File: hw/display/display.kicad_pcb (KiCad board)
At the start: 4 copper layers, 37 x 29 mm, 22 parts, among them J1 Input, J2 Output, U1 SN65LVDS822, U2 SN74LVC00ARGY

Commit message: temp commit for merge
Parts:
- added C13: 0.1uF, Capacitor_SMD:C_0603_1608Metric, F.Cu at (106.5, 77.8)
- added J3: Touch, Connector_FFC-FPC:Hirose_FH12-8S-0.5SH_1x08-1MP_P0.50mm_Horizontal, B.Cu at (108.4, 76.3)
- added J4: Spacer, footprints:Spacer, F.Cu at (145.5, 78.0)
- added J5: Spacer, footprints:Spacer, F.Cu at (145.5, 88.8)
- added R2: DNP, Resistor_SMD:R_0603_1608Metric, F.Cu at (118.5, 74.4)
- added R3: DNP, Resistor_SMD:R_0603_1608Metric, F.Cu at (118.5, 75.9)
- added R4: DNP, Resistor_SMD:R_0603_1608Metric, F.Cu at (118.5, 77.4)
- added R5: DNP, Resistor_SMD:R_0603_1608Metric, F.Cu at (117.2, 95.9)
- added R6: DNP, Resistor_SMD:R_0603_1608Metric, F.Cu at (115.7, 95.9)
- J1: footprint Connector_FFC-FPC:Hirose_FH12-26S-0.5SH_1x26-1MP_P0.50mm_Horizontal -> Connector_Molex:Molex_SlimStack_55560-0301_2x15_P0.50mm_Vertical
- J2: value Output -> Display; moved to B.Cu
- JP3: footprint Jumper:SolderJumper-2_P1.3mm_Bridged_RoundedPad1.0x1.5mm -> Jumper:SolderJumper-3_P1.3mm_Bridged12_RoundedPad1.0x1.5mm
- U2: footprint Package_DFN_QFN:Texas_S-PVQFN-N14_ThermalVias -> footprints:Texas_S-PVQFN-N14_ThermalVias
- moved C11 6.60 mm to (112.0, 81.8), turned to 180 degrees
- moved J2 3.00 mm to (139.1, 94.5)
- moved JP3 1.99 mm to (133.4, 98.5), turned to 0 degrees
- moved J1 1.75 mm to (114.8, 87.8), turned to 90 degrees
- moved C15 1.68 mm to (123.5, 97.2), turned to 270 degrees
- moved R1 1.68 mm to (125.0, 97.2)
- moved C14 0.75 mm to (129.8, 96.5)
- moved U2 0.75 mm to (128.2, 99.6)
- moved C12 0.25 mm to (138.6, 104.2)
- renumbered C13 to C14, C14 to C15
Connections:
- J1 pad 10: /LVDS_A2N -> /LVDS_A1N
- J1 pad 11: /LVDS_A2P -> CTP.RST
- J1 pad 12: GND -> /LVDS_A1P
- J1 pad 13: /LVDS_CLKN -> GND
- J1 pad 14: /LVDS_CLKP -> GND
- J1 pad 15: GND -> SPI.CS
- J1 pad 16: /LVDS_A3N -> /LVDS_A2N
- J1 pad 17: /LVDS_A3P -> SPI.SCK
- J1 pad 18: GND -> /LVDS_A2P
- J1 pad 19: SPI.CS -> SPI.MOSI
- J1 pad 20: SPI.SCK -> GND
- J1 pad 21: SPI.MOSI -> SPI.MISO
- J1 pad 22: SPI.MISO -> /LVDS_CLKN
- J1 pad 24: GND -> /LVDS_CLKP
- J1 pad 25: LED_K -> GND
- J1 pad 26: LED_A -> GND
- J1 pad 3: GND -> Net-(J1-Pad3)
- J1 pad 5: /LVDS_A0P -> CTP.SCL
- J1 pad 6: GND -> /LVDS_A0P
- J1 pad 7: /LVDS_A1N -> CTP.SDA
- J1 pad 8: /LVDS_A1P -> GND
- J1 pad 9: GND -> CTP.INT
- JP3 pad 1: /DISP_EN_IC -> Net-(JP3-Pad1)
- JP3 pad 2: Net-(JP3-Pad2) -> /DISP_DE_INV
- U1 pad 38: /DISP_EN_IC -> /DISP_DE_INV
- U2 pad 10: Net-(JP3-Pad2) -> Net-(JP3-Pad1)
- U2 pad 9: Net-(JP3-Pad2) -> Net-(JP3-Pad1)
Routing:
- net CTP.INT: track 0.00 -> 23.8 mm, vias 0 -> 2
- net CTP.RST: track 0.00 -> 22.6 mm, vias 0 -> 1
- net CTP.SDA: track 0.00 -> 22.0 mm, vias 0 -> 2
- net CTP.SCL: track 0.00 -> 20.8 mm, vias 0 -> 2
- net /DISP_EN_IC: track 16.4 -> 0.00 mm
- net /DISP_DE_INV: track 0.00 -> 16.4 mm
- net LED_A: track 56.0 -> 64.5 mm, vias 0 -> 1
- net /DISP_VSYNC: track 36.7 -> 28.5 mm, vias 2 -> 1
- net /DISP_HSYNC: track 35.0 -> 27.2 mm, vias 2 -> 1
- net /DISP_DE: track 31.5 -> 23.9 mm, vias 2 -> 1
- net /DISP_PCLK: track 33.3 -> 25.8 mm, vias 2 -> 1
- net ENABLE: track 19.9 -> 27.2 mm
- net +3V3: track 31.6 -> 38.8 mm, vias 10 -> 18
- net SPI.MOSI: track 31.8 -> 38.8 mm, vias 0 -> 1
- net SPI.MISO: track 31.8 -> 38.8 mm, vias 0 -> 1
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- added copper zone on F.Cu, net +3V3
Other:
- board size 37 x 29 mm -> 42.8 x 37.6 mm

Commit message: HW REV 3.0
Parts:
- removed JP3: DE INVERT, Jumper:SolderJumper-3_P1.3mm_Bridged12_RoundedPad1.0x1.5mm
- U2: value SN74LVC00ARGY -> 74LVC2G00; footprint footprints:Texas_S-PVQFN-N14_ThermalVias -> Package_SO:VSSOP-8_2.3x2mm_P0.5mm
- moved C14 3.94 mm to (127.8, 99.9)
- moved U2 2.33 mm to (128.6, 97.3), turned to 180 degrees
- moved JP2 2.02 mm to (117.5, 100.0)
- moved C15 0.71 mm to (124.1, 97.7), turned to 90 degrees
- moved R1 0.71 mm to (125.6, 97.7), turned to 90 degrees
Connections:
- U1 pad 38: /DISP_DE_INV -> /DISP_DE
- U2 pad 3: Net-(U2-Pad3) -> /DISP_RST
- U2 pad 4: ENABLE -> GND
- U2 pad 5: Net-(U2-Pad3) -> ENABLE
- U2 pad 6: /DISP_RST -> Net-(U2-Pad6)
- U2 pad 7: GND -> Net-(U2-Pad6)
- U2 pad 8: /DISP_DE -> +3V3
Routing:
- net /DISP_DE_INV: track 16.4 -> 0.00 mm
- net /DISP_RST: track 17.6 -> 12.0 mm
- net Net-(C15-Pad1): track 5.66 -> 10.4 mm
- net /DISP_DE: track 23.9 -> 28.6 mm
- net Net-(JP3-Pad1): track 3.48 -> 0.00 mm
- net Net-(U2-Pad3): track 3.23 -> 0.00 mm, vias 2 -> 0
- net SPI.SCK: track 38.9 -> 36.7 mm
- net SPI.MISO: track 38.8 -> 36.5 mm
- net SPI.MOSI: track 38.8 -> 36.6 mm
- net SPI.CS: track 39.0 -> 36.8 mm
- net ENABLE: track 27.2 -> 25.0 mm
- net Net-(JP2-Pad2): track 13.6 -> 11.6 mm
- net GND: track 67.1 -> 65.9 mm, vias 22 -> 21
- net LED_A: track 64.5 -> 63.3 mm
- net LED_K: track 59.4 -> 58.2 mm
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
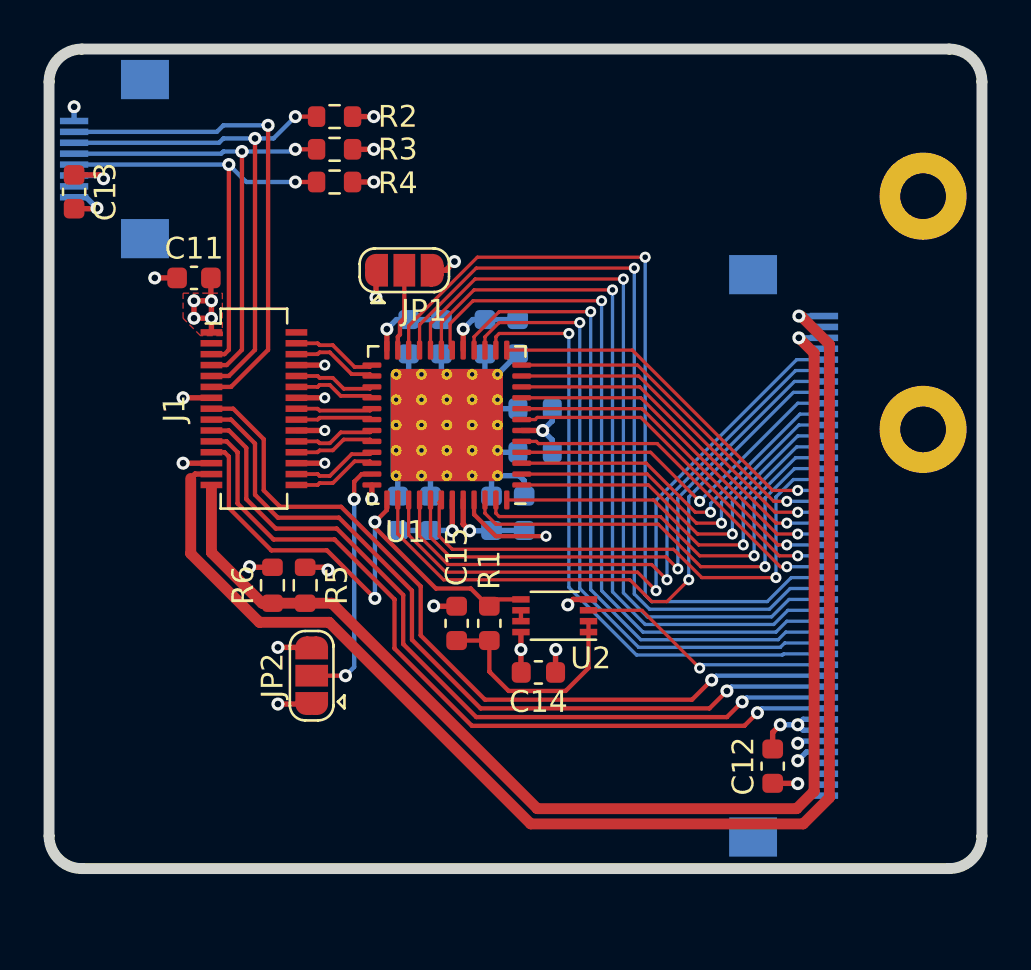
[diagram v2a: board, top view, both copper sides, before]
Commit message: REV3.1:  - fixed audio  - added spacers  - UART is routed through audio mux instead of I2C  - proper display connector alignment
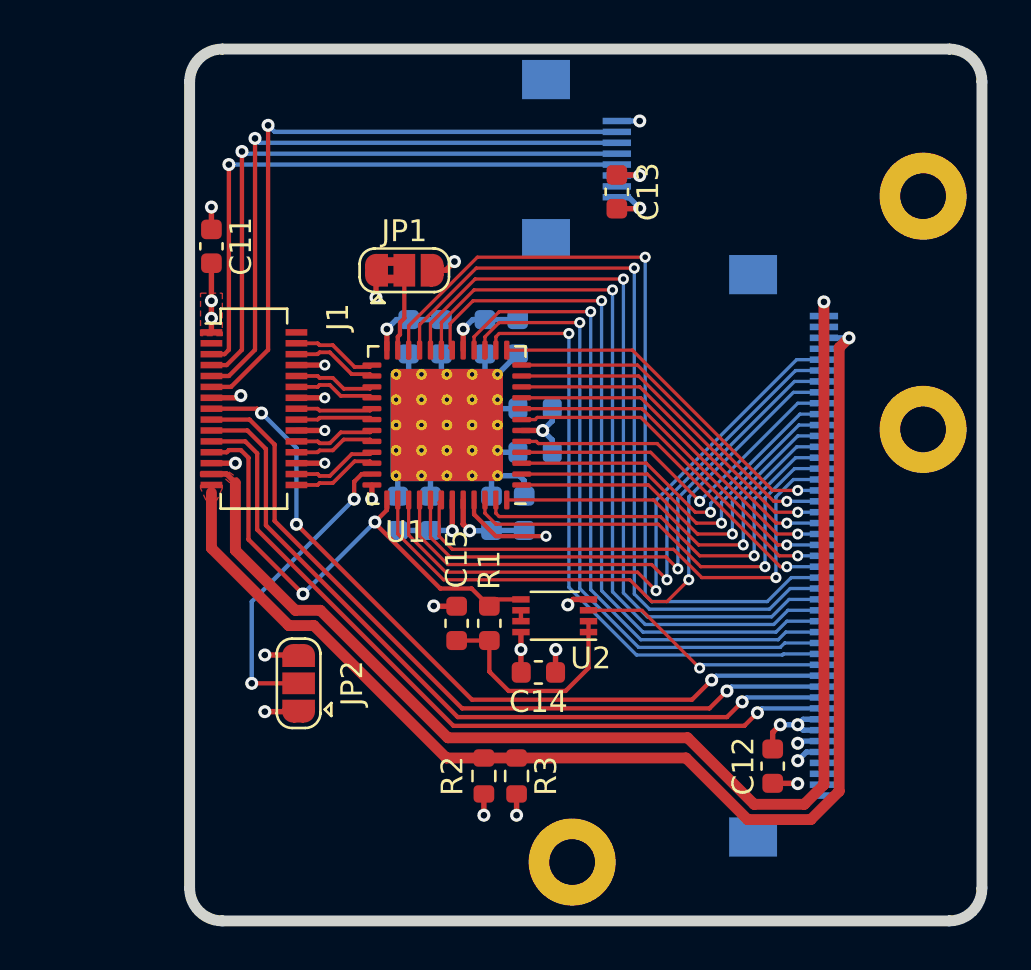
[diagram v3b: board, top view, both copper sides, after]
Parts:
- removed the R2 at (118.5, 74.4)
- removed the R3 at (118.5, 75.9)
- removed R4: DNP, Resistor_SMD:R_0603_1608Metric
- added J6: Spacer, footprints:Spacer, F.Cu at (129.4, 108.6)
- JP1: footprint Jumper:SolderJumper-3_P1.3mm_Open_RoundedPad1.0x1.5mm -> Jumper:SolderJumper-3_P1.3mm_Bridged2Bar12_RoundedPad1.0x1.5mm
- U2: value 74LVC2G00 -> 74AUP2G132DC
- moved C13 24.9 mm to (131.4, 77.8)
- moved J3 21.2 mm to (129.6, 76.3), turned to 90 degrees
- moved R3 14.2 mm to (126.8, 104.7), turned to 270 degrees
- moved R2 12.0 mm to (125.3, 104.7), turned to 270 degrees
- moved C11 1.66 mm to (112.8, 80.3), turned to 90 degrees
- moved JP2 0.69 mm to (116.8, 100.4)
- renumbered R5 to R2, R6 to R3
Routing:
- net CTP.RST: track 22.6 -> 29.7 mm
- net CTP.SCL: track 20.8 -> 27.2 mm, vias 2 -> 1
- net CTP.SDA: track 22.0 -> 28.0 mm, vias 2 -> 1
- net +3V3: track 38.6 -> 33.2 mm, vias 18 -> 13
- net CTP.INT: track 23.8 -> 28.9 mm, vias 2 -> 1
- net LED_A: track 63.3 -> 59.4 mm
- net Net-(JP2-Pad2): track 11.6 -> 14.3 mm
- net ENABLE: track 25.0 -> 23.6 mm
- net LED_K: track 58.2 -> 59.5 mm
- net SPI.MOSI: track 36.6 -> 36.0 mm
- net SPI.MISO: track 36.5 -> 35.9 mm
- net SPI.CS: track 36.8 -> 36.1 mm, vias 1 -> 3
- net SPI.SCK: track 36.7 -> 36.1 mm
- added copper zone on F.Cu, net LED_A
- added copper zone on F.Cu, net LED_K
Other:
- board size 42.8 x 37.6 mm -> 36.3 x 40 mm
